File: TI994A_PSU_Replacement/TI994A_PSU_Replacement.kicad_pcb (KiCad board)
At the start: 2 copper layers, 120 x 106 mm, 18 parts, among them J1 Power In, J2 Power Out, Q1 SUP53P06-20-E3, SW1 SW_Slide_DPDT, U1 R-78CK5.0-0.5, U2 DFR0831

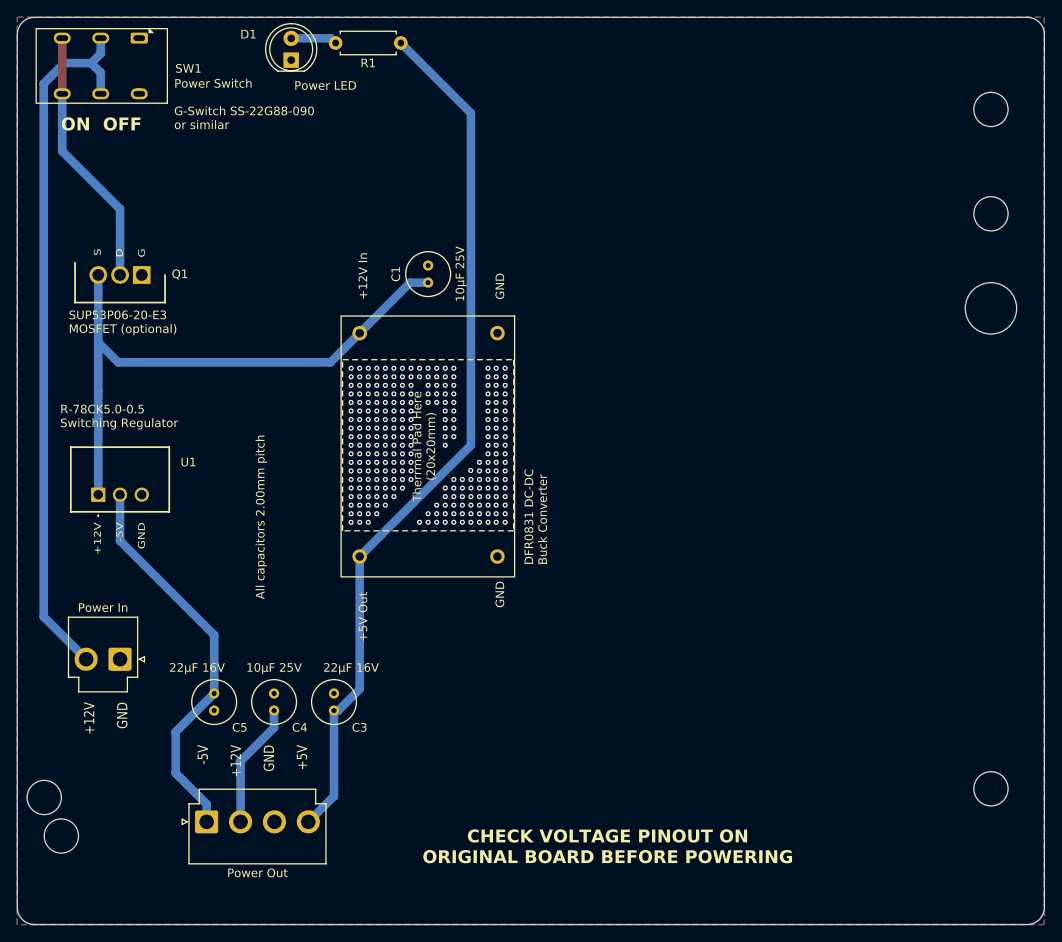
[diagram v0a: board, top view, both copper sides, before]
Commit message: PCB text improvements
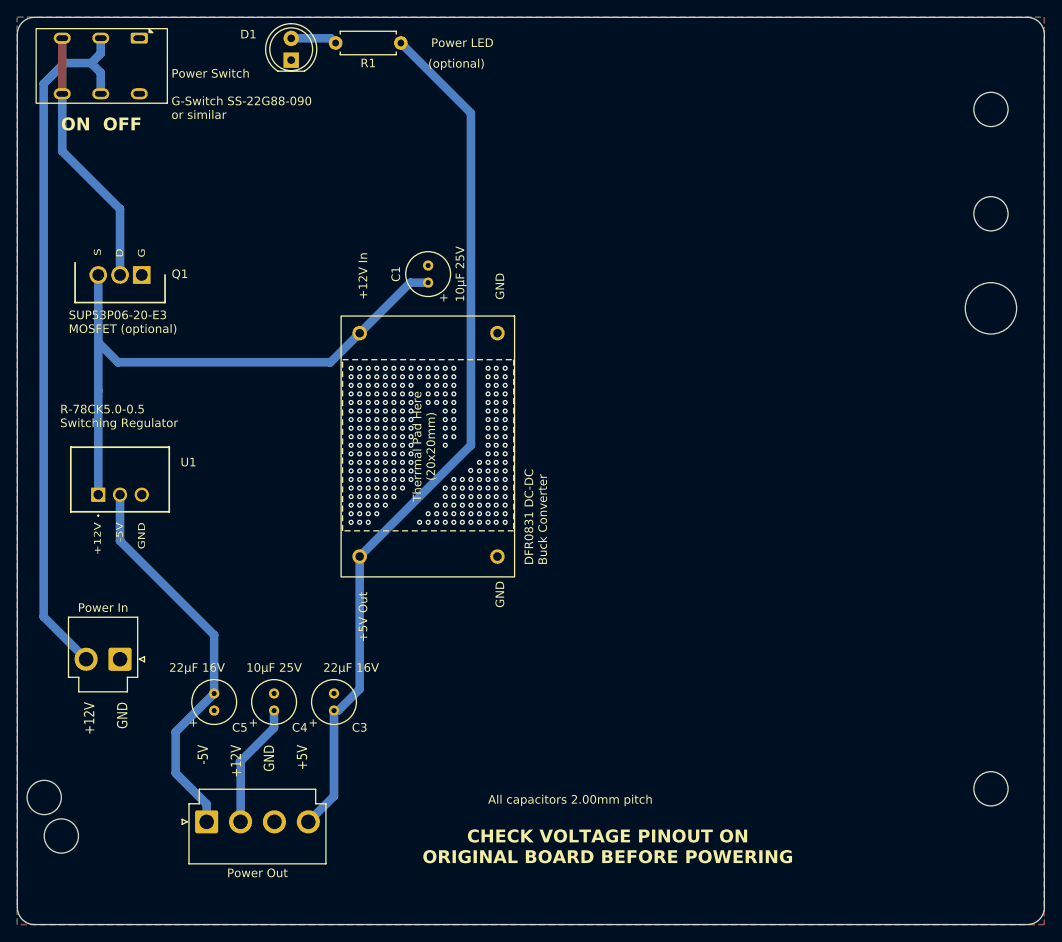
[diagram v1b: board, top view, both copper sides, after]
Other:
- board text added: "(optional)"
- board text added: "+"
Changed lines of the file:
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@@
 		)
 		(property "Value" "Power LED"
-			(at -3 4 180)
+			(at 2 20 180)
 			(layer "F.SilkS")
 			(effects
@@
 			(unlocked yes)
 			(layer "F.SilkS")
+			(hide yes)
 			(effects
 				(font
@@
 		)
 	)
+	(gr_text "+"
+		(at 127.262273 82.332311 0)
+		(layer "F.SilkS")
+		(effects
+			(font
+				(size 1 1)
+				(thickness 0.1)
+			)
+			(justify left bottom)
+		)
+	)
 	(gr_text "+12V\n\nGND"
 		(at 91 129 90)
@@
 		)
 	)
+	(gr_text "+"
+		(at 105 132 0)
+		(layer "F.SilkS")
+		(effects
+			(font
+				(size 1 1)
+				(thickness 0.1)
+			)
+			(justify left bottom)
+		)
+	)
 	(gr_text "DFR0831 DC-DC \nBuck Converter"
 		(at 140 113 90)
@@
 	)
 	(gr_text "All capacitors 2.00mm pitch"
-		(at 107 117 90)
+		(at 133 141 0)
+		(layer "F.SilkS")
+		(effects
+			(font
+				(size 1 1)
+				(thickness 0.15)
+			)
+			(justify left bottom)
+		)
+	)
+	(gr_text "(optional)"
+		(at 126 55 0)
 		(layer "F.SilkS")
 		(effects
@@
 		)
 	)
+	(gr_text "+"
+		(at 98 132 0)
+		(layer "F.SilkS")
+		(effects
+			(font
+				(size 1 1)
+				(thickness 0.1)
+			)
+			(justify left bottom)
+		)
+	)
 	(gr_text "ON  OFF"
 		(at 83.09 62.39 0)
@@
 		)
 	)
+	(gr_text "+"
+		(at 112 132 0)
+		(layer "F.SilkS")
+		(effects
+			(font
+				(size 1 1)
+				(thickness 0.1)
+			)
+			(justify left bottom)
+		)
+	)
 	(gr_text "Power Switch\n\nG-Switch SS-22G88-090\nor similar"
-		(at 96.32 62.17 0)
+		(at 96 61 0)
 		(layer "F.SilkS")
 		(effects
@@
 		)
 	)
-	(gr_text_box "TI 99/4A PSU Replacement Board\nThis version by Brett Hallen (Nov 2025)\nwww.youtube.com/@Brfff\n\nBased on modified version by dabone (2024)\nhttps://github.com/dabonetn\n\nOriginal design by Johnny Blanchard\nhttps://re-enthused.com"
+	(gr_text_box "TI 99/4A PSU Replacement Board (Rev. A)\nThis version by Brett Hallen (Nov 2025)\nwww.youtube.com/@Brfff\n\nBased on modified version by dabone (2024)\nhttps://github.com/dabonetn\n\nOriginal design by Johnny Blanchard\nhttps://re-enthused.com"
 		(start 153.112363 79.169318)
 		(end 178 136.830681)

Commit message: Added missing +12V track
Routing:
- net +12V: track 83.7 -> 132.0 mm
- net GND: vias 263 -> 261
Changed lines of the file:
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@@
 		(allow_soldermask_bridges_in_footprints no)
 		(tenting front back)
-		(grid_origin 78 49)
+		(grid_origin 129.007434 104.995919)
 		(pcbplotparams
 			(layerselection 0x00000000_00000000_55555555_5755f5ff)
@@
 	)
 	(gr_text "Therrmal Pad Here\n(20x20mm)"
-		(at 126.931 99.14 90)
+		(at 127.2 99.2 90)
 		(layer "F.SilkS")
 		(effects
@@
 	)
 	(via
-		(at 129 103)
-		(size 0.6)
-		(drill 0.3)
-		(layers "F.Cu" "B.Cu")
-		(free yes)
-		(net 1)
-	)
-	(via
 		(at 117 99)
 		(size 0.6)
@@
 	)
 	(via
-		(at 128 104)
-		(size 0.6)
-		(drill 0.3)
-		(layers "F.Cu" "B.Cu")
-		(free yes)
-		(net 1)
-	)
-	(via
 		(at 135 103)
 		(size 0.6)
@@
 	)
 	(segment
+		(start 108 130)
+		(end 106.007434 128.007434)
+		(width 1)
+		(layer "B.Cu")
+		(net 2)
+	)
+	(segment
 		(start 87.46 104.775)
 		(end 87.46 92.65)
@@
 	)
 	(segment
+		(start 106.007434 128.007434)
+		(end 106.007434 105.547434)
+		(width 1)
+		(layer "B.Cu")
+		(net 2)
+	)
+	(segment
 		(start 104 136)
 		(end 104.08 136.08)
@@
 	)
 	(segment
+		(start 106.007434 105.547434)
+		(end 89.78 89.32)
+		(width 1)
+		(layer "B.Cu")
+		(net 2)
+	)
+	(segment
 		(start 131 60.19)
 		(end 122.81 52)
@@
 	)
 	(segment
-		(start 131 99)
-		(end 131 60.19)
+		(start 118 112)
+		(end 118 127)
 		(width 1)
 		(layer "B.Cu")
@@
 	)
 	(segment
-		(start 118 112)
-		(end 118 127.5)
+		(start 131 99)
+		(end 131 60.19)
 		(width 1)
 		(layer "B.Cu")
@@
 	)
 	(segment
-		(start 118 127.5)
-		(end 115.5 130)
+		(start 118 127)
+		(end 115 130)
 		(width 1)
 		(layer "B.Cu")
@@
 		(width 1)
 		(layer "B.Cu")
-		(net 3)
-	)
-	(segment
-		(start 115.5 130)
-		(end 115 130)
-		(width 1)
-		(layer "B.Cu")
